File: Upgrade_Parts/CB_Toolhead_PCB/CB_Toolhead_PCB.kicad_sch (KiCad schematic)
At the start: 10 parts, among them J1 Micro-Fit, J10 JST-3, J2 JST-4, J4 JST-2, J5 JST-2, J6 JST-2, J7 JST-2, J8 JST-2

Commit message: minor toolhead pcb update
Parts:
- J2: footprint (none) -> Connector_JST:JST_EH_B4B-EH-A_1x04_P2.50mm_Vertical
- J?: footprint Connector_JST:JST_EH_B3B-EH-A_1x03_P2.50mm_Vertical -> (none)
- TH1: value 100k_PTC -> Semitec 104GT2
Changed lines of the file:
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@@
       (effects (font (size 1.27 1.27)) hide)
     )
-    (property "Datasheet" "~" (id 3) (at 214.63 116.84 0)
+    (property "Datasheet" "https://www.digikey.ch/de/products/detail/jst-sales-america-inc/B3B-XH-A-LF-SN/1651046" (id 3) (at 214.63 116.84 0)
       (effects (font (size 1.27 1.27)) hide)
     )
@@
       (effects (font (size 1.27 1.27)) hide)
     )
-    (property "Datasheet" "~" (id 3) (at 214.63 57.15 0)
+    (property "Datasheet" "https://www.digikey.ch/de/products/detail/jst-sales-america-inc/B2B-XH-A-GU/2043065" (id 3) (at 214.63 57.15 0)
       (effects (font (size 1.27 1.27)) hide)
     )
@@
       (effects (font (size 1.27 1.27)) (justify left))
     )
-    (property "Footprint" "" (id 2) (at 125.73 77.47 0)
-      (effects (font (size 1.27 1.27)) hide)
-    )
-    (property "Datasheet" "~" (id 3) (at 125.73 77.47 0)
+    (property "Footprint" "Connector_JST:JST_EH_B4B-EH-A_1x04_P2.50mm_Vertical" (id 2) (at 125.73 77.47 0)
+      (effects (font (size 1.27 1.27)) hide)
+    )
+    (property "Datasheet" "https://www.digikey.ch/de/products/detail/jst-sales-america-inc/B4B-XH-A-LF-SN/1651047" (id 3) (at 125.73 77.47 0)
       (effects (font (size 1.27 1.27)) hide)
     )
@@
       (effects (font (size 1.27 1.27)) hide)
     )
-    (property "Datasheet" "~" (id 3) (at 214.63 69.85 0)
+    (property "Datasheet" "https://www.digikey.ch/de/products/detail/jst-sales-america-inc/B2B-XH-A-GU/2043065" (id 3) (at 214.63 69.85 0)
       (effects (font (size 1.27 1.27)) hide)
     )
@@
       (effects (font (size 1.27 1.27)) (justify left))
     )
-    (property "Footprint" "Connector_JST:JST_EH_B3B-EH-A_1x03_P2.50mm_Vertical" (id 2) (at 214.63 97.79 0)
-      (effects (font (size 1.27 1.27)) hide)
-    )
-    (property "Datasheet" "~" (id 3) (at 214.63 97.79 0)
+    (property "Footprint" "" (id 2) (at 214.63 97.79 0)
+      (effects (font (size 1.27 1.27)) hide)
+    )
+    (property "Datasheet" "" (id 3) (at 214.63 97.79 0)
       (effects (font (size 1.27 1.27)) hide)
     )
@@
       (effects (font (size 1.27 1.27)) hide)
     )
-    (property "Datasheet" "~" (id 3) (at 93.98 77.47 0)
+    (property "Datasheet" "https://www.digikey.ch/de/products/detail/molex/0430451612/531412" (id 3) (at 93.98 77.47 0)
       (effects (font (size 1.27 1.27)) hide)
     )
@@
       (effects (font (size 1.27 1.27)) hide)
     )
-    (property "Datasheet" "~" (id 3) (at 214.63 82.55 0)
+    (property "Datasheet" "https://www.digikey.ch/de/products/detail/jst-sales-america-inc/B2B-XH-A-GU/2043065" (id 3) (at 214.63 82.55 0)
       (effects (font (size 1.27 1.27)) hide)
     )
@@
       (effects (font (size 1.27 1.27)) hide)
     )
-    (property "Datasheet" "~" (id 3) (at 214.63 44.45 0)
+    (property "Datasheet" "https://www.digikey.ch/de/products/detail/jst-sales-america-inc/B2B-XH-A-GU/2043065" (id 3) (at 214.63 44.45 0)
       (effects (font (size 1.27 1.27)) hide)
     )
@@
       (effects (font (size 1.27 1.27)) (justify left))
     )
-    (property "Value" "100k_PTC" (id 1) (at 123.19 95.5674 0)
+    (property "Value" "Semitec 104GT2" (id 1) (at 123.19 95.5674 0)
       (effects (font (size 1.27 1.27)) (justify left))
     )
@@
       (effects (font (size 1.27 1.27)) (justify left) hide)
     )
-    (property "Datasheet" "~" (id 3) (at 120.65 93.98 0)
+    (property "Datasheet" "https://eu.mouser.com/ProductDetail/Semitec/104GT-2?qs=wgO0AD0o1vvQ2Rm%2FPgvFdg%3D%3D" (id 3) (at 120.65 93.98 0)
       (effects (font (size 1.27 1.27)) hide)
     )
@@
       (effects (font (size 1.27 1.27)) hide)
     )
-    (property "Datasheet" "~" (id 3) (at 214.63 127 0)
+    (property "Datasheet" "https://www.digikey.ch/de/products/detail/jst-sales-america-inc/B2B-XH-A-GU/2043065" (id 3) (at 214.63 127 0)
       (effects (font (size 1.27 1.27)) hide)
     )
@@
     )
     (path "/94d38031-c802-49a1-b705-ef20f9bacdc3"
-      (reference "J2") (unit 1) (value "JST-4") (footprint "")
+      (reference "J2") (unit 1) (value "JST-4") (footprint "Connector_JST:JST_EH_B4B-EH-A_1x04_P2.50mm_Vertical")
     )
     (path "/bf88d3d1-7516-4904-93c3-302c3cbbbe08"
@@
     )
     (path "/b51c2137-5172-45b1-b385-ffd3192fbee3"
-      (reference "J?") (unit 1) (value "Endstop") (footprint "Connector_JST:JST_EH_B3B-EH-A_1x03_P2.50mm_Vertical")
+      (reference "J?") (unit 1) (value "Endstop") (footprint "")
     )
     (path "/c5d90d50-8815-42b3-bdfe-855c387da089"
-      (reference "TH1") (unit 1) (value "100k_PTC") (footprint "Resistor_THT:R_Axial_DIN0207_L6.3mm_D2.5mm_P10.16mm_Horizontal")
-    )
-  )
+      (reference "TH1") (unit 1) (value "Semitec 104GT2") (footprint "Resistor_THT:R_Axial_DIN0207_L6.3mm_D2.5mm_P10.16mm_Horizontal")
+    )
+  )

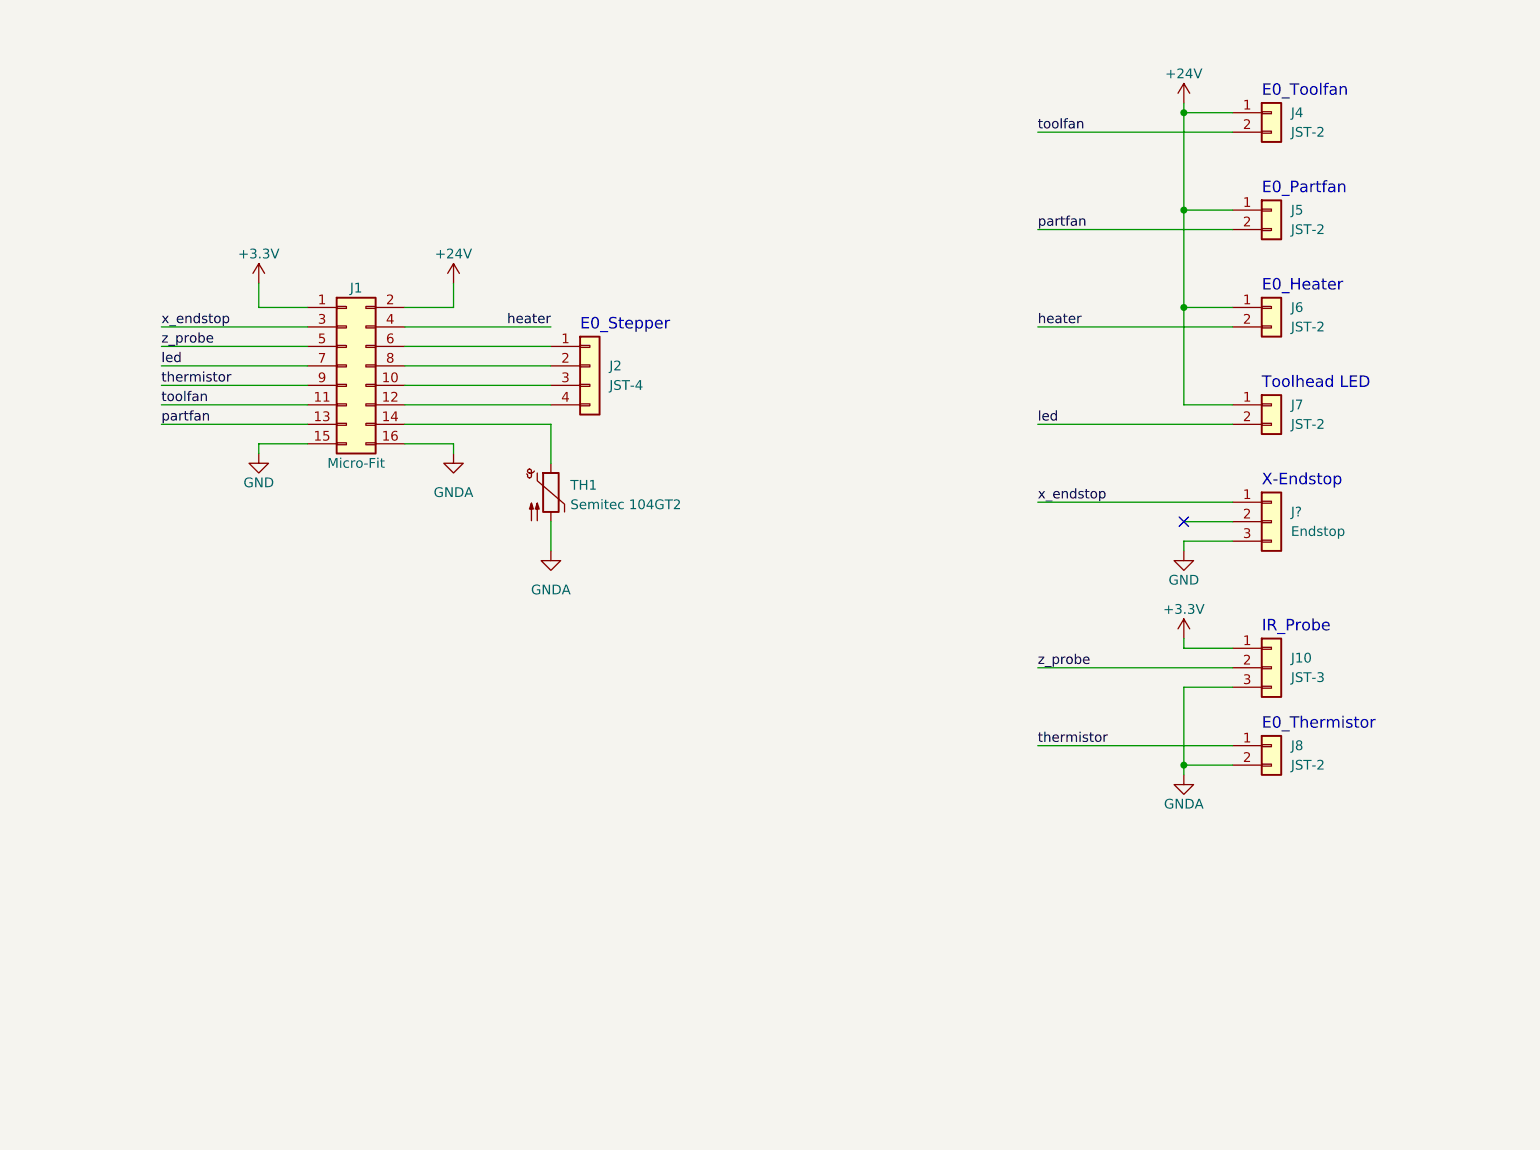
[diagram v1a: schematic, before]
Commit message: added LIS3DH
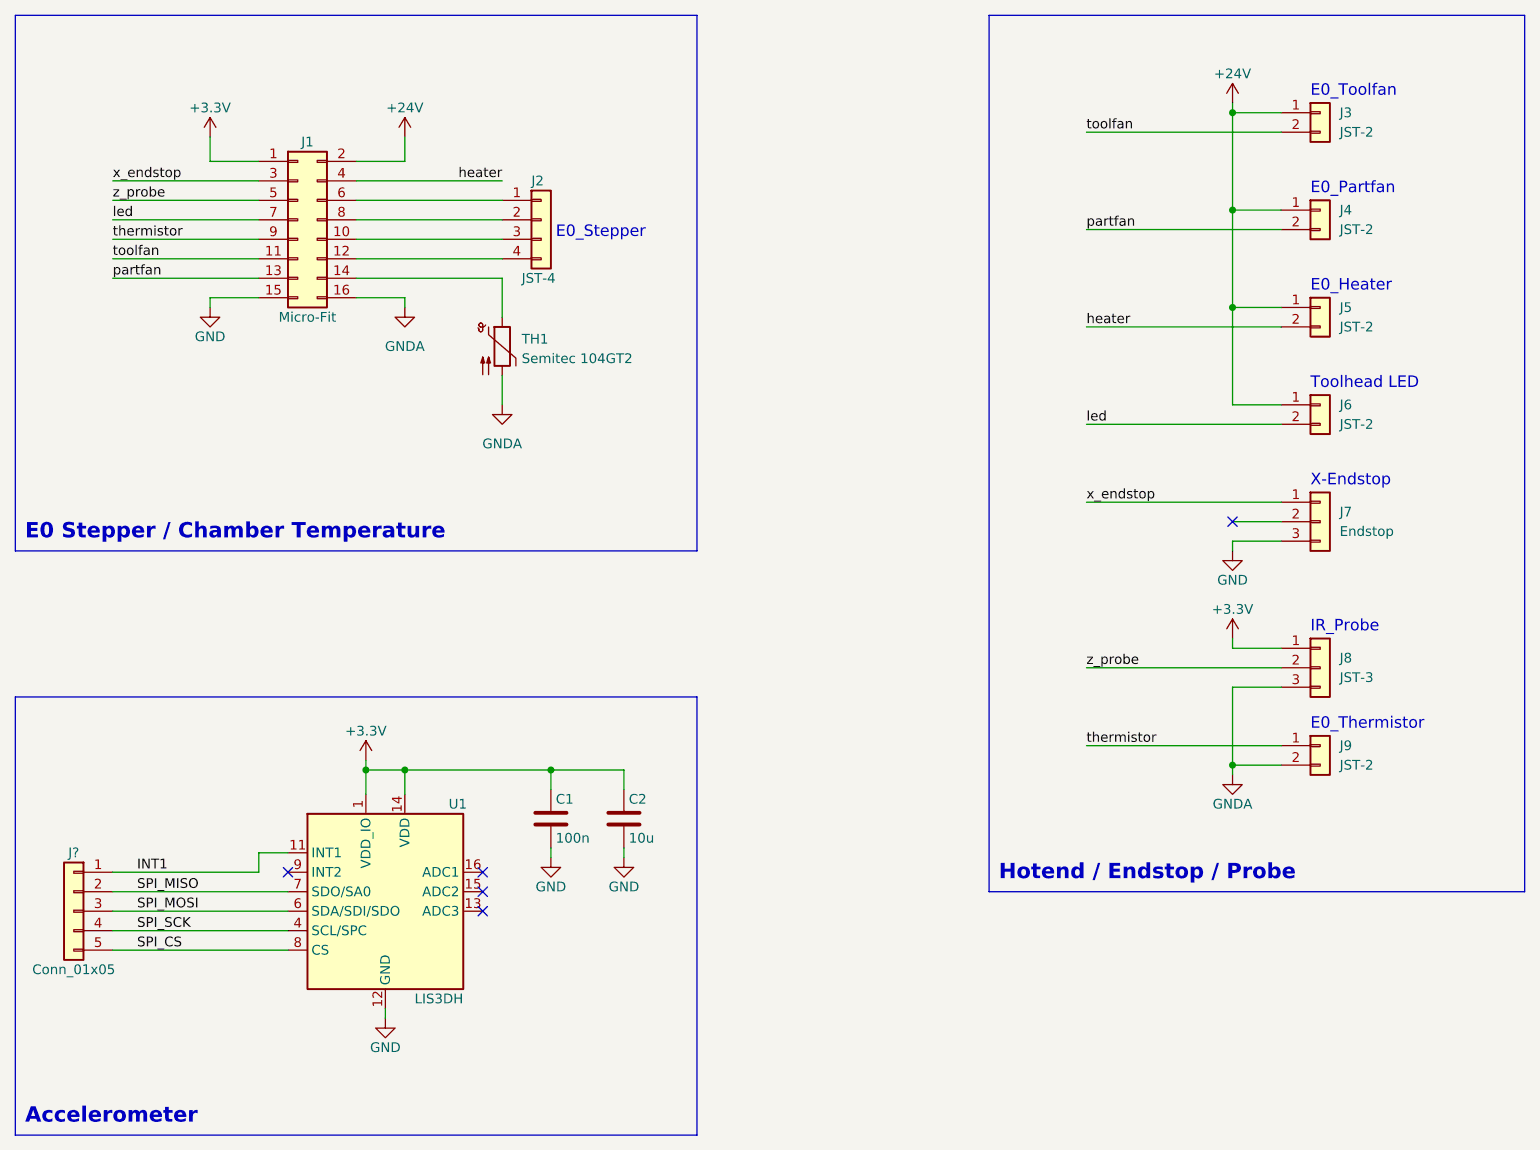
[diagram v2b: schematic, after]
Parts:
- added C1: 100n, symbol Device:C
- added C2: 10u, symbol Device:C
- added J?: Conn_01x05, symbol Connector_Generic:Conn_01x05
- added U1: LIS3DH, Package_LGA:LGA-16_3x3mm_P0.5mm_LayoutBorder3x5y, symbol Sensor_Motion:LIS3DH
- gave numbers to parts that had none: 1
- renumbered J4 to J3, J5 to J4, J6 to J5, J7 to J6, J10 to J8, J8 to J9
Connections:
- net +3V3: now also C1.1, C2.1, U1.1 (VDD_IO), U1.14 (VDD)
- net GND: now also C1.2, C2.2, U1.10 (GND), U1.12 (GND), U1.5 (GND)
- new net INT1: J?.1 (Pin_1), U1.11 (INT1)
- new net SPI_CS: J?.5 (Pin_5), U1.8 (CS)
- new net SPI_MISO: J?.2 (Pin_2), U1.7 (SDO/SA0)
- new net SPI_MOSI: J?.3 (Pin_3), U1.6 (SDA/SDI/SDO)
- new net SPI_SCK: J?.4 (Pin_4), U1.4 (SCL/SPC)
- no-connect marks 1 -> 5
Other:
- note added: "Accelerometer"
- note added: "E0 Stepper / Chamber Temperature"
- note added: "Hotend / Endstop / Probe"
- moved on the sheet: J1, J2, J3, J4, J5, J6, J7, J8, J9, TH1
